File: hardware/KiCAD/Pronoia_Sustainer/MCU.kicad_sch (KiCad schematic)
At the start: 9 parts, among them Q6 AO3400A, U2 Teensy4.1

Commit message: updated Schematics
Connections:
- net PyroSense0: now also U2.29 (37_CS); no longer U2.33 (41_A17)
- net PyroSense1: now also U2.28 (36_CS); no longer U2.32 (40_A16)
- net PyroSense2: now also U2.27 (35_TX8); no longer U2.31 (39_MISO1_OUT1A)
- net PyroSense3: now also U2.26 (34_RX8); no longer U2.30 (38_CS1_IN1)
- net PyroSense4: now also U2.25 (33_MCLK2); no longer U2.29 (37_CS)
- net Vbatt_Monitor: now also U2.33 (41_A17)
- net RGB_LED: now reaches R28.1
- net RGB_LED: now also U2.31 (39_MISO1_OUT1A)
- net UI_Buzzer: now reaches R26.1
- net UI_Buzzer: now also U2.32 (40_A16)
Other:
- note added: "Analog Pin Input"
- note removed: "Analog Pin"
- moved on the sheet: C14, D6, LS1, Q6, R25, R26, R27, R28

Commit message: Completed 1st draft of Schematic
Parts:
- LS1: LCSC (none) -> C76871
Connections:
- net GND: now also U2.1 (GND), U2.34 (GND), U2.52 (GND), U2.58 (GND), U2.59 (GND), U2.64 (GND)
- net Pyro4: no longer names the net of U2.45 (23_A9_CRX1_MCLK1)
- net PyroSense4: no longer names the net of U2.25 (33_MCLK2)
- no-connect marks 1 -> 26
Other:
- note added: "Teensy 4.1 Header Connection"
- moved on the sheet: LS1, Q6, R25, R26, R27

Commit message: Last commit for KiCAD schematic w/ GPS, Telem, and Bluetooth
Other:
- company: (none) -> Walla Walla University
- title: (none) -> Pronoia Sustainer Flight Computer
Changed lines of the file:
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@@
 	(generator_version "9.0")
 	(paper "A4")
+	(title_block
+		(title "Pronoia Sustainer Flight Computer")
+		(date "2026-02-03")
+		(rev "1.0")
+		(company "Walla Walla University")
+		(comment 1 "Prometheus Rocket Project")
+	)
 	(text "Parts Not Shown"
 		(exclude_from_sim no)

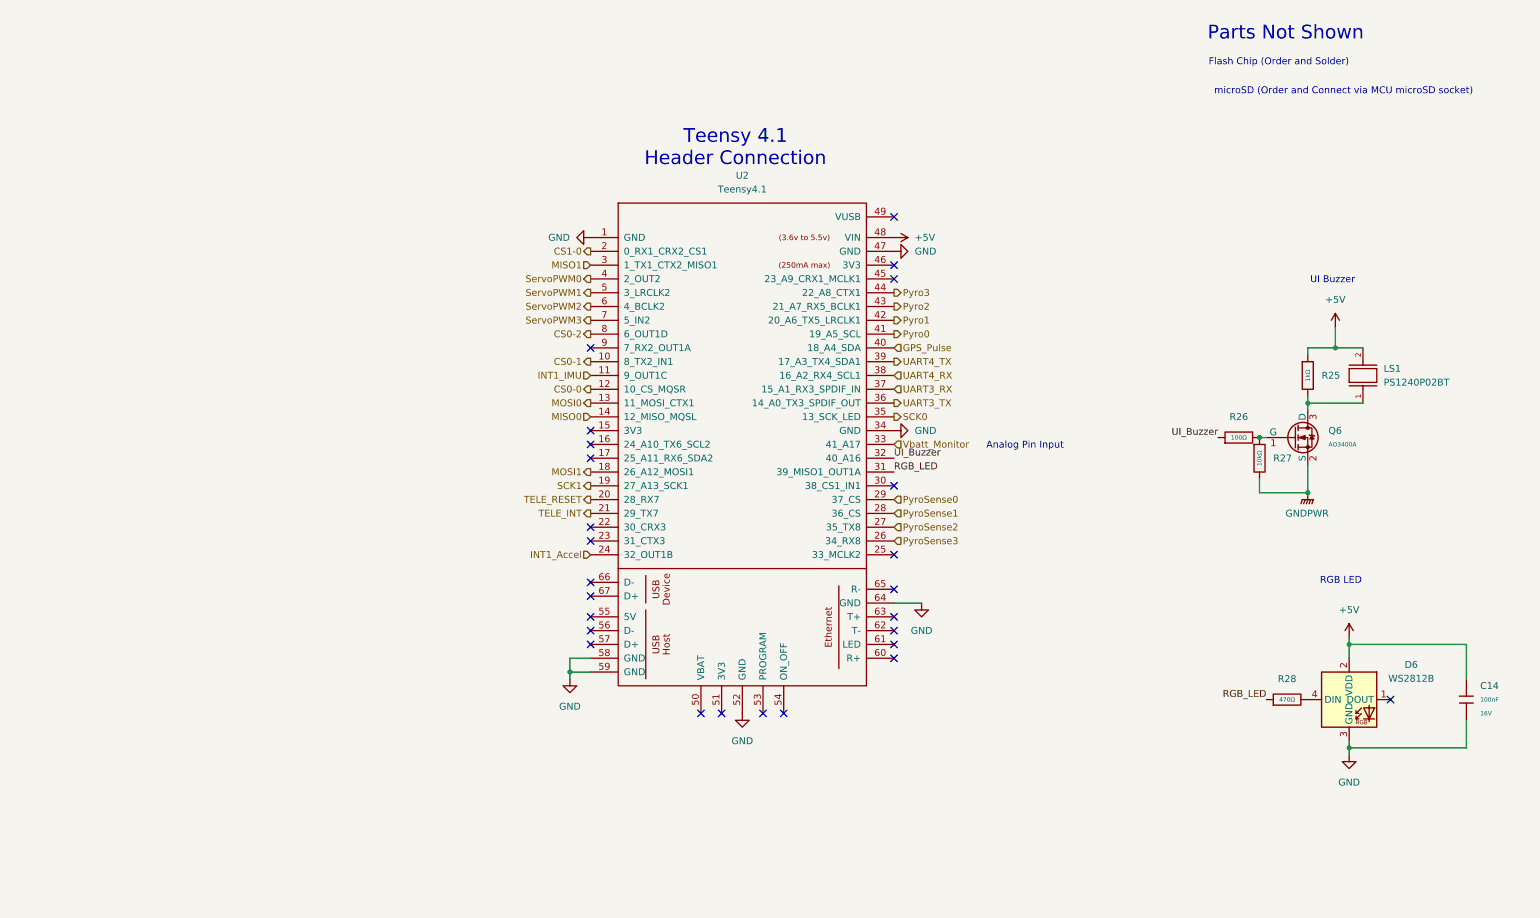
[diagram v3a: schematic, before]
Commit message: Red LED and UI Buzzer Circuit
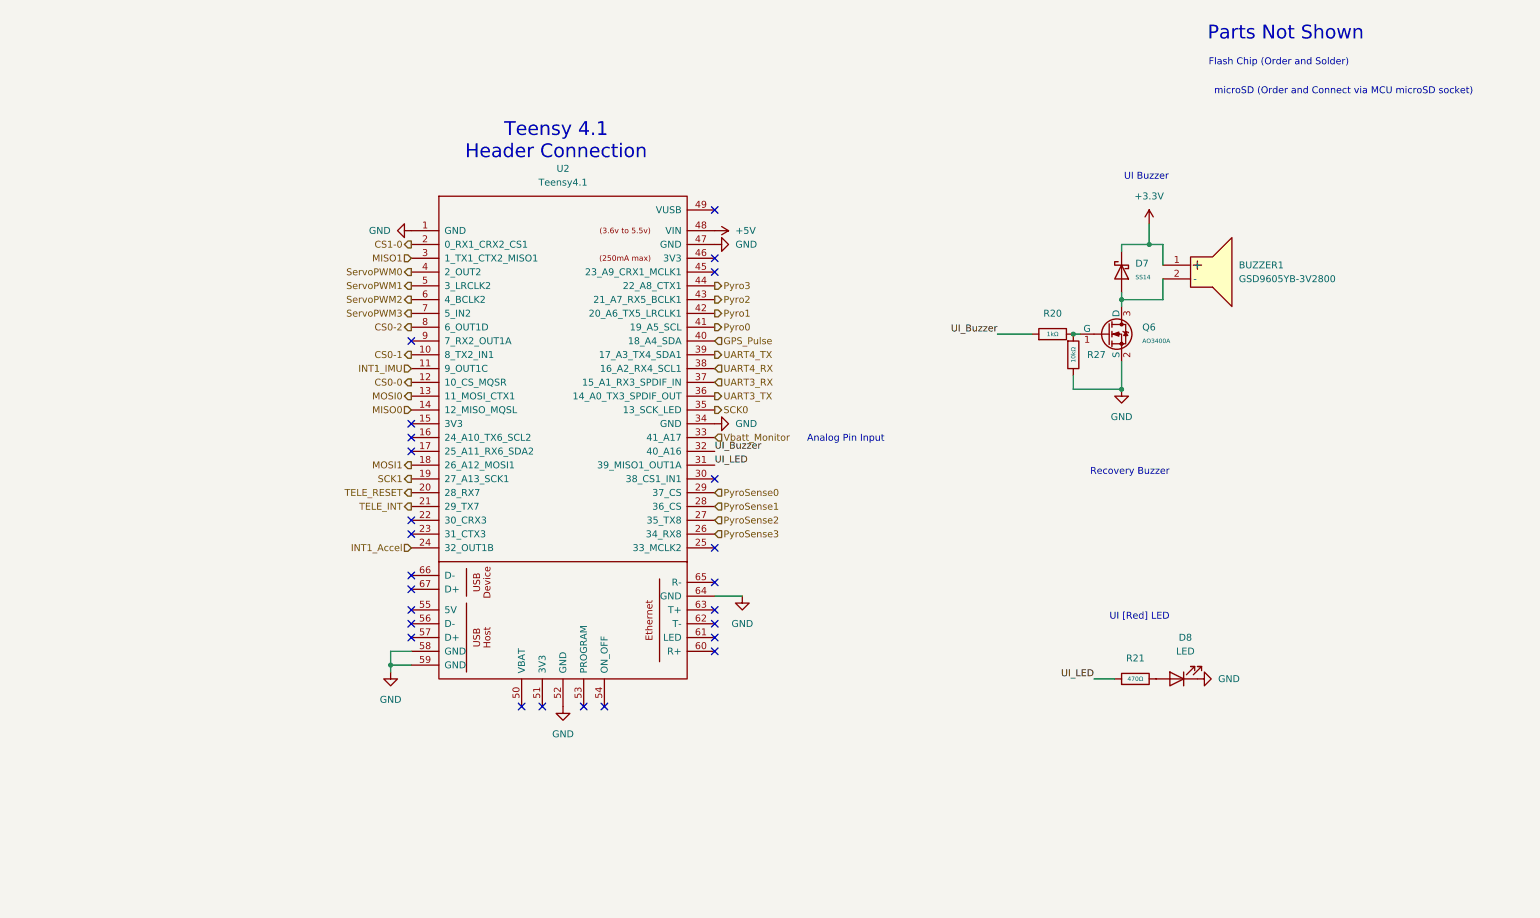
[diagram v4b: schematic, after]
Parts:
- removed C14: 100nF, PCM_JLCPCB:C_0402, symbol PCM_JLCPCB-Capacitors:0402,100nF
- removed D6: WS2812B, PCM_JLCPCB:LED-SMD_4P-L1.6-W1.5_XL-1615RGBC-WS2812B, symbol PCM_JLCPCB-Extended:LED, WS2812B, 1615
- removed LS1: PS1240P02BT, PS1240P02BT:XDCR_PS1240P02BT, symbol PS1240P02BT:PS1240P02BT
- removed R25: 1kΩ, PCM_JLCPCB:R_0805, symbol PCM_JLCPCB-Resistors:0805,1kΩ
- removed R26: 100Ω, PCM_JLCPCB:R_0805, symbol PCM_JLCPCB-Resistors:0805,100Ω
- removed R28: 470Ω, PCM_JLCPCB:R_0402, symbol PCM_JLCPCB-Resistors:0402,470Ω
- added BUZZER1: GSD9605YB-3V2800, GSD9605YB-3V2800:BUZ-SMD_GSD9605YB-3V2800, symbol GSD9605YB-3V2800:GSD9605YB-3V2800
- added D7: SS14, PCM_JLCPCB:D_SMA, symbol PCM_JLCPCB-Diodes:Schottky,SS14
- added D8: LED, symbol Device:LED
- added R20: 1kΩ, PCM_JLCPCB:R_0805, symbol PCM_JLCPCB-Resistors:0805,1kΩ
- added R21: 470Ω, PCM_JLCPCB:R_0402, symbol PCM_JLCPCB-Resistors:0402,470Ω
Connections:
- net GNDPWR is gone; now on net GND: Q6.2 (S), R27.2
- net GND: now also D8.1 (K)
- net UI_Buzzer: now also R20.1
- net at Q6.1 (G), R27.1: now also R20.2
- net at Q6.3 (D): now also BUZZER1.2 (-), D7.2
- net RGB_LED renamed UI_LED
- net UI_LED: now also R21.1
- new net: D8.2 (A), R21.2
- new net +3.3V: BUZZER1.1 (+), D7.1
- no-connect marks 26 -> 25
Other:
- note added: "Recovery Buzzer"
- note added: "UI [Red] LED"
- note removed: "RGB LED"
- moved on the sheet: Q6, R27, U2

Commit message: Finalized v2.0 of Pronoia Schematic
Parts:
- added C14: 22uF, PCM_JLCPCB:C_0805, symbol PCM_JLCPCB-Capacitors:0805,22uF
- added J11: 640457-2, 640457-2:TE_640457-2, symbol 640457-2:640457-2
- added J12, J14: Conn_01x24_Pin, Connector_PinSocket_2.54mm:PinSocket_1x24_P2.54mm_Vertical, symbol Connector:Conn_01x24_Pin
- added Q5: AO3400A, PCM_JLCPCB:Q_SOT-23, symbol PCM_JLCPCB-Transistors:NMOS,AO3400A
- added R22: 1kΩ, PCM_JLCPCB:R_0805, symbol PCM_JLCPCB-Resistors:0805,1kΩ
- added R25: 10kΩ, PCM_JLCPCB:R_0805, symbol PCM_JLCPCB-Resistors:0805,10kΩ
- added R26, R28, R35, R36: 33Ω, PCM_JLCPCB:R_0402, symbol PCM_JLCPCB-Resistors:0402,33Ω
- D8: footprint (none) -> LED_SMD:LED_0603_1608Metric; LCSC (none) -> C3030991
- U2: now not fitted
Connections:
- net +3.3V: now also C14.1, J14.3 (Pin_3)
- net +5V: now also J14.1 (Pin_1); no longer U2.48 (VIN)
- net CS0-0: now also J12.13 (Pin_13); no longer U2.12 (10_CS_MQSR)
- net CS0-1: now also J14.20 (Pin_20); no longer U2.10 (8_TX2_IN1)
- net CS1-0: now also J12.23 (Pin_23); no longer U2.2 (0_RX1_CRX2_CS1)
- net GND: now also C14.2, J12.24 (Pin_24), J14.15 (Pin_15), J14.2 (Pin_2), Q5.2 (S), R25.2; no longer U2.1 (GND), U2.34 (GND), U2.47 (GND), U2.52 (GND), U2.58 (GND), U2.59 (GND), U2.64 (GND)
- net INT1_Accel: now also J12.14 (Pin_14); no longer U2.24 (32_OUT1B)
- net INT1_IMU: now also J12.15 (Pin_15); no longer U2.11 (9_OUT1C)
- net MISO0: now also J12.11 (Pin_11); no longer U2.14 (12_MISO_MQSL)
- net MISO1: now also J12.22 (Pin_22); no longer U2.3 (1_TX1_CTX2_MISO1)
- net MOSI0: now also R28.1; no longer U2.13 (11_MOSI_CTX1)
- net MOSI1: now also R35.1; no longer U2.18 (26_A12_MOSI1)
- net Pyro0: now also J14.19 (Pin_19); no longer U2.41 (19_A5_SCL)
- net Pyro1: now also J14.18 (Pin_18); no longer U2.42 (20_A6_TX5_LRCLK1)
- net Pyro2: now also J14.17 (Pin_17); no longer U2.43 (21_A7_RX5_BCLK1)
- net Pyro3: now also J14.16 (Pin_16); no longer U2.44 (22_A8_CTX1)
- net PyroSense0: now also J14.21 (Pin_21); no longer U2.29 (37_CS)
- net PyroSense1: now also J14.22 (Pin_22); no longer U2.28 (36_CS)
- net PyroSense2: now also J14.23 (Pin_23); no longer U2.27 (35_TX8)
- net PyroSense3: now also J14.24 (Pin_24); no longer U2.26 (34_RX8)
- net SCK0: now also R26.2; no longer U2.35 (13_SCK_LED)
- net SCK1: now also R36.1; no longer U2.19 (27_A13_SCK1)
- net ServoPWM0: now also J12.9 (Pin_9); no longer U2.4 (2_OUT2)
- net ServoPWM1: now also J12.8 (Pin_8); no longer U2.5 (3_LRCLK2)
- net ServoPWM2: now also J12.5 (Pin_5); no longer U2.6 (4_BCLK2)
- net ServoPWM3: now also J12.4 (Pin_4); no longer U2.7 (5_IN2)
- net UI_Buzzer: now also J12.18 (Pin_18); no longer U2.32 (40_A16)
- net UI_LED: now also J12.19 (Pin_19); no longer U2.31 (39_MISO1_OUT1A)
- net Vbatt_Monitor: now also J14.13 (Pin_13); no longer U2.33 (41_A17)
- net CS0-2: no longer names the net of U2.8 (6_OUT1D)
- net GPS_Pulse: no longer names the net of U2.40 (18_A4_SDA)
- net TELE_INT: no longer names the net of U2.21 (29_TX7)
- net TELE_RESET: no longer names the net of U2.20 (28_RX7)
- net UART3_RX: no longer names the net of U2.37 (15_A1_RX3_SPDIF_IN)
- net UART3_TX: no longer names the net of U2.36 (14_A0_TX3_SPDIF_OUT)
- net UART4_RX: no longer names the net of U2.38 (16_A2_RX4_SCL1)
- net UART4_TX: no longer names the net of U2.39 (17_A3_TX4_SDA1)
- new net: Q5.1 (G), R22.2, R25.1
- new net: J11.2, Q5.3 (D)
- new net: J12.7 (Pin_7), R35.2
- new net: J14.14 (Pin_14), R26.1
- new net: J12.12 (Pin_12), R28.2
- new net: J12.6 (Pin_6), R36.2
- new net GX-12-4_Detect: J14.9 (Pin_9)
- new net RecoveryBuzzPower: J11.1
- new net Recovery_Buzzer: J12.20 (Pin_20), R22.1
- new net UART1_RX: J14.11 (Pin_11)
- new net UART1_TX: J14.10 (Pin_10)
- no-connect marks 25 -> 80
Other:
- note added: "Recovery Buzzer connected via Screw Terminal Block"
- note added: "Swiss Pin Male and Female Headers for Teensy 4.1"
- note added: "Teensy 4.1 Swiss Pin Header Connection"
- note removed: "Teensy 4.1 Header Connection"
- note removed: "microSD (Order and Connect via MCU microSD socket)"
- moved on the sheet: D7, D8, Q6, R20, R21, R27

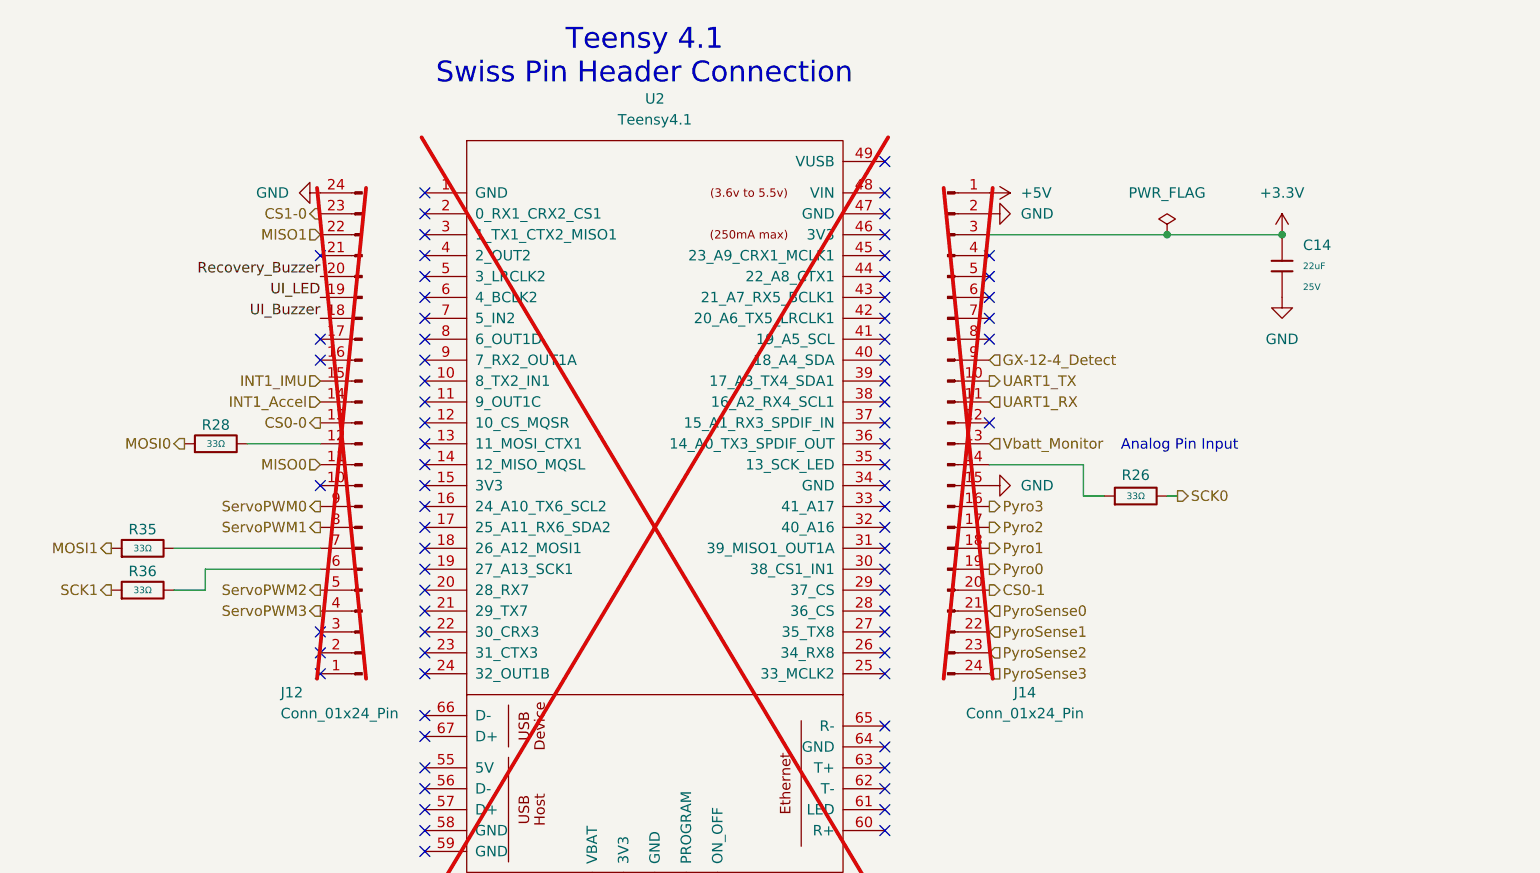
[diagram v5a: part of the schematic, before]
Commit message: Finished PCB layout
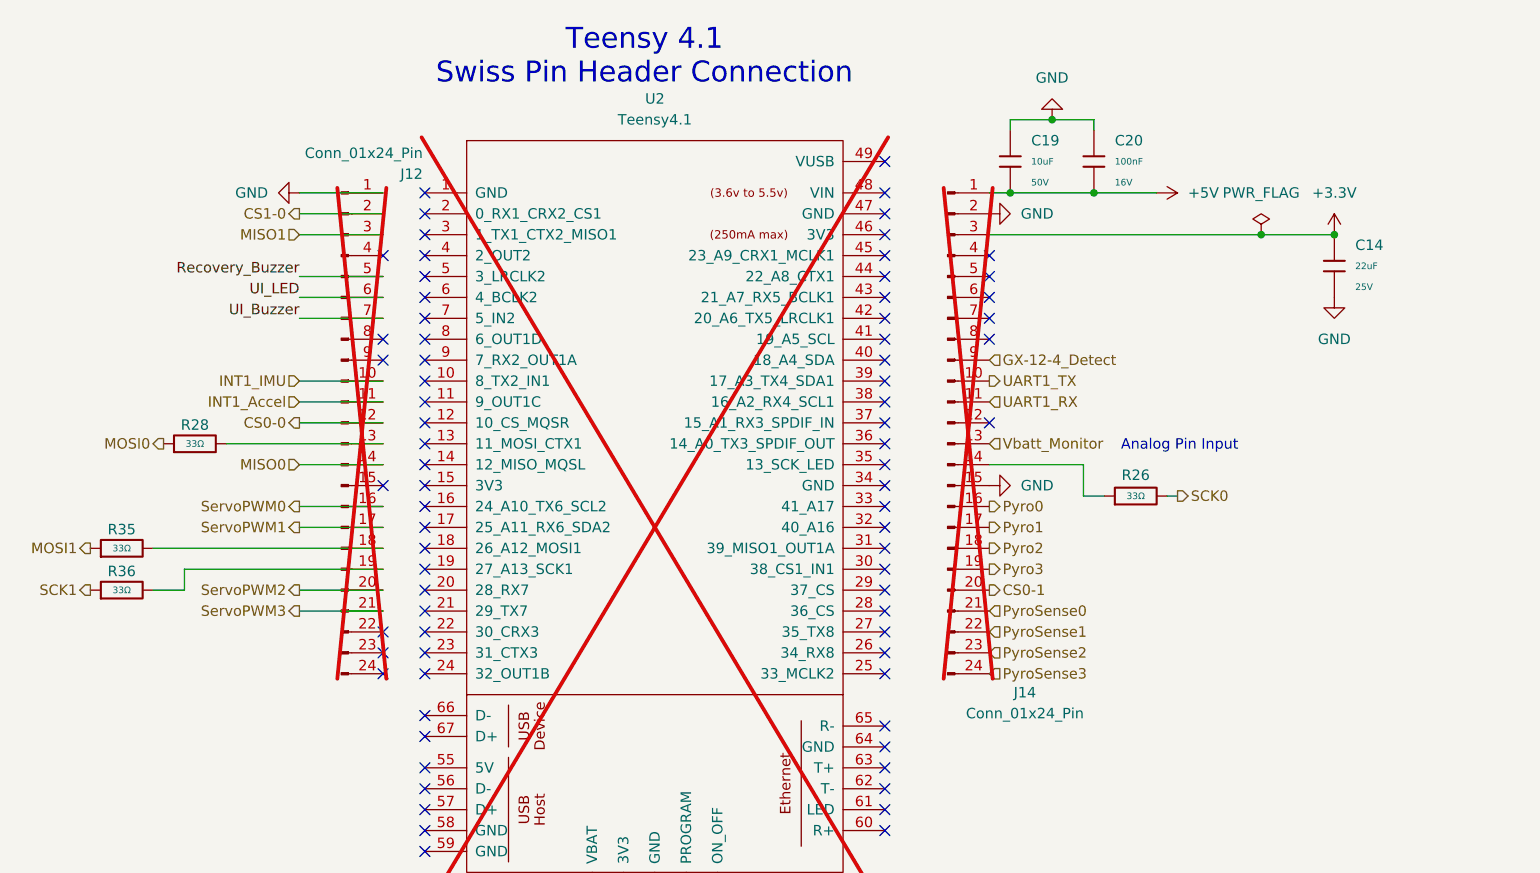
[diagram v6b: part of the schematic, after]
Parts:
- added C19: 10uF, PCM_JLCPCB:C_1206, symbol PCM_JLCPCB-Capacitors:1206,10uF
- added C20: 100nF, PCM_JLCPCB:C_0402, symbol PCM_JLCPCB-Capacitors:0402,100nF
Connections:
- net +5V: now also C19.2, C20.1
- net CS0-0: now also J12.12 (Pin_12); no longer J12.13 (Pin_13)
- net CS1-0: now also J12.2 (Pin_2); no longer J12.23 (Pin_23)
- net GND: now also J12.1 (Pin_1), C19.1, C20.2; no longer J12.24 (Pin_24)
- net INT1_Accel: now also J12.11 (Pin_11); no longer J12.14 (Pin_14)
- net INT1_IMU: now also J12.10 (Pin_10); no longer J12.15 (Pin_15)
- net MISO0: now also J12.14 (Pin_14); no longer J12.11 (Pin_11)
- net MISO1: now also J12.3 (Pin_3); no longer J12.22 (Pin_22)
- net Pyro0: now also J14.16 (Pin_16); no longer J14.19 (Pin_19)
- net Pyro1: now also J14.17 (Pin_17); no longer J14.18 (Pin_18)
- net Pyro2: now also J14.18 (Pin_18); no longer J14.17 (Pin_17)
- net Pyro3: now also J14.19 (Pin_19); no longer J14.16 (Pin_16)
- net Recovery_Buzzer: now also J12.5 (Pin_5); no longer J12.20 (Pin_20)
- net ServoPWM0: now also J12.16 (Pin_16); no longer J12.9 (Pin_9)
- net ServoPWM1: now also J12.17 (Pin_17); no longer J12.8 (Pin_8)
- net ServoPWM2: now also J12.20 (Pin_20); no longer J12.5 (Pin_5)
- net ServoPWM3: now also J12.21 (Pin_21); no longer J12.4 (Pin_4)
- net UI_Buzzer: now also J12.7 (Pin_7); no longer J12.18 (Pin_18)
- net UI_LED: now also J12.6 (Pin_6); no longer J12.19 (Pin_19)
- net at R35.2: now also J12.18 (Pin_18); no longer J12.7 (Pin_7)
- net at R28.2: now also J12.13 (Pin_13); no longer J12.12 (Pin_12)
- net at R36.2: now also J12.19 (Pin_19); no longer J12.6 (Pin_6)
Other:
- moved on the sheet: C14, J12, R28, R35, R36

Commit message: Sensor Bring-Up
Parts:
- BUZZER1: LCSC (none) -> C255327; LCSC Part C255327 -> (none)
- J11, J12, J14, U2: now left out of the parts list
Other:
- moved on the sheet: C14

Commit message: Updated codebase
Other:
- note added: "Servo Motor A"
- note added: "Servo Motor B"
- note added: "Servo Motor C"
- note added: "Servo Motor D"
- moved on the sheet: C14, C19, C20, J12, J14, R26, R28, R35, R36, U2
